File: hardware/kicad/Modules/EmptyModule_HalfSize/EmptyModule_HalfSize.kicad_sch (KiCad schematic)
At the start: 2 parts, among them J1 Conn_02x04_Odd_Even, J2 Conn_02x04_Odd_Even

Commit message: Updated E,ptyModule, 2 Variants (Full, Half)- Sized
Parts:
- J1, J2: footprint EnvNode:PinSocket_2x04_P2.54mm_Vertical_Bottom -> EnvNode-Footprints:PinSocket_2x04_P2.54mm_Vertical_Bottom
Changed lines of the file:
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@@
 			)
 		)
-		(property "Footprint" "EnvNode:PinSocket_2x04_P2.54mm_Vertical_Bottom"
+		(property "Footprint" "EnvNode-Footprints:PinSocket_2x04_P2.54mm_Vertical_Bottom"
 			(at 58.42 81.28 0)
 			(hide yes)
@@
 		)
 		(instances
-			(project "EmptyModule"
+			(project "EmptyModule_HalfSize"
 				(path "/bef1201e-12b5-4ddb-8361-fbfddd4aa238"
 					(reference "J1")
@@
 		)
 		(instances
-			(project "EmptyModule"
+			(project "EmptyModule_HalfSize"
 				(path "/bef1201e-12b5-4ddb-8361-fbfddd4aa238"
 					(reference "#PWR03")
@@
 			)
 		)
-		(property "Footprint" "EnvNode:PinSocket_2x04_P2.54mm_Vertical_Bottom"
+		(property "Footprint" "EnvNode-Footprints:PinSocket_2x04_P2.54mm_Vertical_Bottom"
 			(at 99.06 81.28 0)
 			(hide yes)
@@
 		)
 		(instances
-			(project "EmptyModule"
+			(project "EmptyModule_HalfSize"
 				(path "/bef1201e-12b5-4ddb-8361-fbfddd4aa238"
 					(reference "J2")
@@
 		)
 		(instances
-			(project "EmptyModule"
+			(project "EmptyModule_HalfSize"
 				(path "/bef1201e-12b5-4ddb-8361-fbfddd4aa238"
 					(reference "#PWR04")

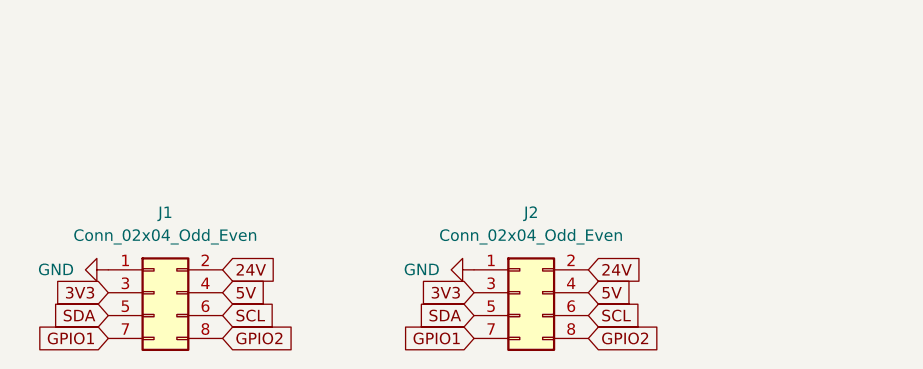
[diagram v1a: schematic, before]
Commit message: feat(hardware): add HalfSize empty module template
- derive HalfSize template from the validated FullSize project
- preserve the linked daughterboard interface design block
- define the 38 x 32 mm board outline and GND zone
- retain standardized connector geometry and routing
- validate pinout, geometry, ERC, and layout structure
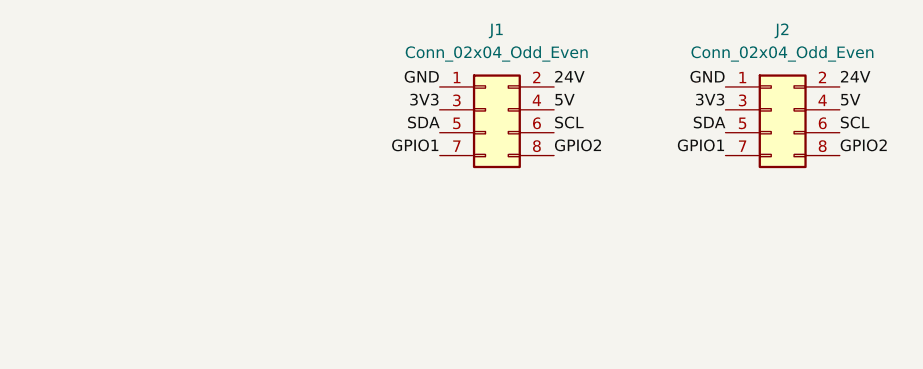
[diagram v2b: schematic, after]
